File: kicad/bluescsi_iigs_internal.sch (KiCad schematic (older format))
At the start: 26 parts, among them J1 Conn_02x13_Odd_Even, J2 Conn_02x13_Odd_Even, J3 105162-0001, J4 Conn_01x02_Male, Q1 Q_PMOS_GSD, SW1 SW_SPDT, U1 YAAJ_BluePill, U2 UC560x, UCC56xx, U3 UC560x, UCC56xx, U4 AMS1117-5.0

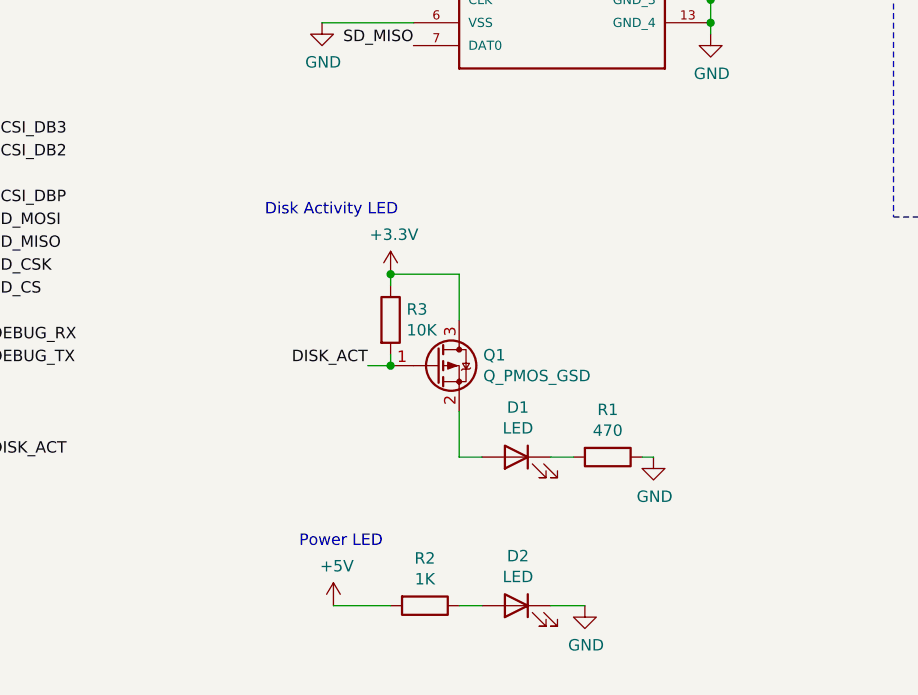
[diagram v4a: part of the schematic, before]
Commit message: Added connector for external activity LED
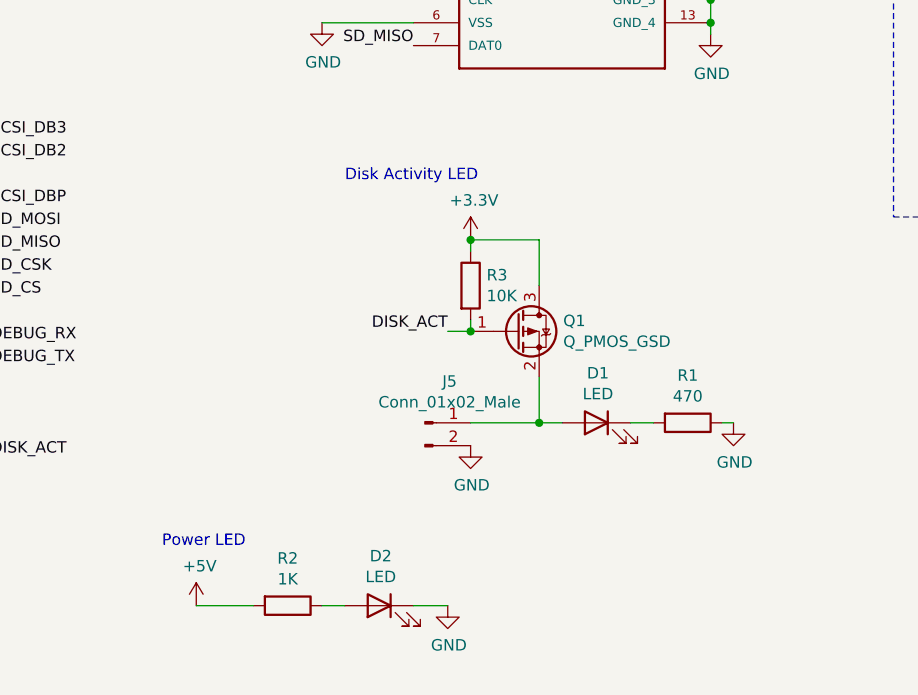
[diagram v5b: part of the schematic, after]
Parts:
- added J5: Conn_01x02_Male, Connector_PinHeader_2.54mm:PinHeader_1x02_P2.54mm_Vertical, symbol Connector:Conn_01x02_Male
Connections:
- net GND: now also J5.2 (Pin_2)
- net at D1.2 (A), Q1.2 (S): now also J5.1 (Pin_1)
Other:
- moved on the sheet: D1, D2, Q1, R1, R2, R3
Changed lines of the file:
@@
 L Device:LED D2
 U 1 1 60631033
-P 5300 7350
-F 0 "D2" H 5293 7567 50  0000 C CNN
-F 1 "LED" H 5293 7476 50  0000 C CNN
-F 2 "LED_SMD:LED_0805_2012Metric_Pad1.15x1.40mm_HandSolder" H 5300 7350 50  0001 C CNN
-F 3 "~" H 5300 7350 50  0001 C CNN
-	1    5300 7350
+P 4700 7350
+F 0 "D2" H 4693 7567 50  0000 C CNN
+F 1 "LED" H 4693 7476 50  0000 C CNN
+F 2 "LED_SMD:LED_0805_2012Metric_Pad1.15x1.40mm_HandSolder" H 4700 7350 50  0001 C CNN
+F 3 "~" H 4700 7350 50  0001 C CNN
+	1    4700 7350
 	-1   0    0    -1
 $EndComp
@@
 L Device:R R2
 U 1 1 60634BDC
-P 4900 7350
-F 0 "R2" V 4693 7350 50  0000 C CNN
-F 1 "1K" V 4784 7350 50  0000 C CNN
-F 2 "Resistor_SMD:R_0805_2012Metric_Pad1.20x1.40mm_HandSolder" V 4830 7350 50  0001 C CNN
-F 3 "~" H 4900 7350 50  0001 C CNN
-	1    4900 7350
+P 4300 7350
+F 0 "R2" V 4093 7350 50  0000 C CNN
+F 1 "1K" V 4184 7350 50  0000 C CNN
+F 2 "Resistor_SMD:R_0805_2012Metric_Pad1.20x1.40mm_HandSolder" V 4230 7350 50  0001 C CNN
+F 3 "~" H 4300 7350 50  0001 C CNN
+	1    4300 7350
 	0    1    1    0
 $EndComp
@@
 L power:GND #PWR0111
 U 1 1 60635DA0
-P 5600 7350
-F 0 "#PWR0111" H 5600 7100 50  0001 C CNN
-F 1 "GND" H 5605 7177 50  0000 C CNN
-F 2 "" H 5600 7350 50  0001 C CNN
-F 3 "" H 5600 7350 50  0001 C CNN
-	1    5600 7350
-	1    0    0    -1
-$EndComp
-Wire Wire Line
-	5450 7350 5600 7350
+P 5000 7350
+F 0 "#PWR0111" H 5000 7100 50  0001 C CNN
+F 1 "GND" H 5005 7177 50  0000 C CNN
+F 2 "" H 5000 7350 50  0001 C CNN
+F 3 "" H 5000 7350 50  0001 C CNN
+	1    5000 7350
+	1    0    0    -1
+$EndComp
+Wire Wire Line
+	4850 7350 5000 7350
 $Comp
 L power:+5V #PWR0113
 U 1 1 60637375
-P 4500 7350
-F 0 "#PWR0113" H 4500 7200 50  0001 C CNN
-F 1 "+5V" H 4515 7523 50  0000 C CNN
-F 2 "" H 4500 7350 50  0001 C CNN
-F 3 "" H 4500 7350 50  0001 C CNN
-	1    4500 7350
-	1    0    0    -1
-$EndComp
-Wire Wire Line
-	4750 7350 4500 7350
+P 3900 7350
+F 0 "#PWR0113" H 3900 7200 50  0001 C CNN
+F 1 "+5V" H 3915 7523 50  0000 C CNN
+F 2 "" H 3900 7350 50  0001 C CNN
+F 3 "" H 3900 7350 50  0001 C CNN
+	1    3900 7350
+	1    0    0    -1
+$EndComp
+Wire Wire Line
+	4150 7350 3900 7350
 $Comp
 L power:GND #PWR0114
@@
 DISK_ACT
 Wire Wire Line
-	5050 7350 5150 7350
-Text Label 4650 6300 2    50   ~ 0
+	4450 7350 4550 7350
+Text Label 5000 6150 2    50   ~ 0
 DISK_ACT
 $Comp
 L Device:R R1
 U 1 1 606332E3
-P 5700 6700
-F 0 "R1" V 5493 6700 50  0000 C CNN
-F 1 "470" V 5584 6700 50  0000 C CNN
-F 2 "Resistor_SMD:R_0805_2012Metric_Pad1.20x1.40mm_HandSolder" V 5630 6700 50  0001 C CNN
-F 3 "~" H 5700 6700 50  0001 C CNN
-	1    5700 6700
+P 6050 6550
+F 0 "R1" V 5843 6550 50  0000 C CNN
+F 1 "470" V 5934 6550 50  0000 C CNN
+F 2 "Resistor_SMD:R_0805_2012Metric_Pad1.20x1.40mm_HandSolder" V 5980 6550 50  0001 C CNN
+F 3 "~" H 6050 6550 50  0001 C CNN
+	1    6050 6550
 	0    1    1    0
 $EndComp
@@
 L Device:LED D1
 U 1 1 60632077
-P 5300 6700
-F 0 "D1" H 5293 6917 50  0000 C CNN
-F 1 "LED" H 5293 6826 50  0000 C CNN
-F 2 "LED_SMD:LED_0805_2012Metric_Pad1.15x1.40mm_HandSolder" H 5300 6700 50  0001 C CNN
-F 3 "~" H 5300 6700 50  0001 C CNN
-	1    5300 6700
+P 5650 6550
+F 0 "D1" H 5643 6767 50  0000 C CNN
+F 1 "LED" H 5643 6676 50  0000 C CNN
+F 2 "LED_SMD:LED_0805_2012Metric_Pad1.15x1.40mm_HandSolder" H 5650 6550 50  0001 C CNN
+F 3 "~" H 5650 6550 50  0001 C CNN
+	1    5650 6550
 	-1   0    0    -1
 $EndComp
-Text Notes 4200 5650 0    50   ~ 0
+Text Notes 4550 5500 0    50   ~ 0
 Disk Activity LED
 Wire Notes Line
@@
 Text Notes 4400 3900 0    50   ~ 0
 MicroSD card slot\nMolex 105162-0001
-Text Notes 4350 7100 0    50   ~ 0
+Text Notes 3750 7100 0    50   ~ 0
 Power LED
 Wire Notes Line
@@
 L Device:Q_PMOS_GSD Q1
 U 1 1 609D8A80
-P 4950 6300
-F 0 "Q1" H 5155 6346 50  0000 L CNN
-F 1 "Q_PMOS_GSD" H 5155 6255 50  0000 L CNN
-F 2 "Package_TO_SOT_SMD:SOT-23" H 5150 6400 50  0001 C CNN
-F 3 "~" H 4950 6300 50  0001 C CNN
-	1    4950 6300
+P 5300 6150
+F 0 "Q1" H 5505 6196 50  0000 L CNN
+F 1 "Q_PMOS_GSD" H 5505 6105 50  0000 L CNN
+F 2 "Package_TO_SOT_SMD:SOT-23" H 5500 6250 50  0001 C CNN
+F 3 "~" H 5300 6150 50  0001 C CNN
+	1    5300 6150
 	1    0    0    -1
 $EndComp
@@
 L power:+3.3V #PWR0126
 U 1 1 609DCA9E
-P 4750 5900
-F 0 "#PWR0126" H 4750 5750 50  0001 C CNN
-F 1 "+3.3V" H 4765 6073 50  0000 C CNN
-F 2 "" H 4750 5900 50  0001 C CNN
-F 3 "" H 4750 5900 50  0001 C CNN
-	1    4750 5900
+P 5100 5750
+F 0 "#PWR0126" H 5100 5600 50  0001 C CNN
+F 1 "+3.3V" H 5115 5923 50  0000 C CNN
+F 2 "" H 5100 5750 50  0001 C CNN
+F 3 "" H 5100 5750 50  0001 C CNN
+	1    5100 5750
 	1    0    0    -1
 $EndComp
@@
 L Device:R R3
 U 1 1 609DE44B
-P 4750 6100
-F 0 "R3" H 4820 6146 50  0000 L CNN
-F 1 "10K" H 4820 6055 50  0000 L CNN
-F 2 "Resistor_SMD:R_0805_2012Metric_Pad1.20x1.40mm_HandSolder" V 4680 6100 50  0001 C CNN
-F 3 "~" H 4750 6100 50  0001 C CNN
-	1    4750 6100
-	1    0    0    -1
-$EndComp
-Wire Wire Line
-	4750 5900 5050 5900
-Wire Wire Line
-	4650 6300 4750 6300
-Wire Wire Line
-	5050 6700 5150 6700
-Wire Wire Line
-	5050 6500 5050 6700
-Wire Wire Line
-	5450 6700 5550 6700
+P 5100 5950
+F 0 "R3" H 5170 5996 50  0000 L CNN
+F 1 "10K" H 5170 5905 50  0000 L CNN
+F 2 "Resistor_SMD:R_0805_2012Metric_Pad1.20x1.40mm_HandSolder" V 5030 5950 50  0001 C CNN
+F 3 "~" H 5100 5950 50  0001 C CNN
+	1    5100 5950
+	1    0    0    -1
+$EndComp
+Wire Wire Line
+	5100 5750 5400 5750
+Wire Wire Line
+	5000 6150 5100 6150
+Wire Wire Line
+	5400 6550 5500 6550
+Wire Wire Line
+	5400 6350 5400 6550
+Wire Wire Line
+	5800 6550 5900 6550
 $Comp
 L power:GND #PWR0127
 U 1 1 609F55CD
-P 5900 6700
-F 0 "#PWR0127" H 5900 6450 50  0001 C CNN
-F 1 "GND" H 5905 6527 50  0000 C CNN
-F 2 "" H 5900 6700 50  0001 C CNN
-F 3 "" H 5900 6700 50  0001 C CNN
-	1    5900 6700
-	1    0    0    -1
-$EndComp
-Wire Wire Line
-	5850 6700 5900 6700
-Wire Wire Line
-	5050 5900 5050 6100
-Wire Wire Line
-	4750 5900 4750 5950
-Connection ~ 4750 5900
-Wire Wire Line
-	4750 6250 4750 6300
-Connection ~ 4750 6300
+P 6250 6550
+F 0 "#PWR0127" H 6250 6300 50  0001 C CNN
+F 1 "GND" H 6255 6377 50  0000 C CNN
+F 2 "" H 6250 6550 50  0001 C CNN
+F 3 "" H 6250 6550 50  0001 C CNN
+	1    6250 6550
+	1    0    0    -1
+$EndComp
+Wire Wire Line
+	6200 6550 6250 6550
+Wire Wire Line
+	5400 5750 5400 5950
+Wire Wire Line
+	5100 5750 5100 5800
+Connection ~ 5100 5750
+Wire Wire Line
+	5100 6100 5100 6150
+Connection ~ 5100 6150
+$Comp
+L Connector:Conn_01x02_Male J5
+U 1 1 60AA760E
+P 4900 6550
+F 0 "J5" H 5008 6731 50  0000 C CNN
+F 1 "Conn_01x02_Male" H 5008 6640 50  0000 C CNN
+F 2 "Connector_PinHeader_2.54mm:PinHeader_1x02_P2.54mm_Vertical" H 4900 6550 50  0001 C CNN
+F 3 "~" H 4900 6550 50  0001 C CNN
+	1    4900 6550
+	1    0    0    -1
+$EndComp
+Wire Wire Line
+	5100 6550 5400 6550
+Connection ~ 5400 6550
+$Comp
+L power:GND #PWR0128
+U 1 1 60AA99DB
+P 5100 6650
+F 0 "#PWR0128" H 5100 6400 50  0001 C CNN
+F 1 "GND" H 5105 6477 50  0000 C CNN
+F 2 "" H 5100 6650 50  0001 C CNN
+F 3 "" H 5100 6650 50  0001 C CNN
+	1    5100 6650
+	1    0    0    -1
+$EndComp
 $EndSCHEMATC

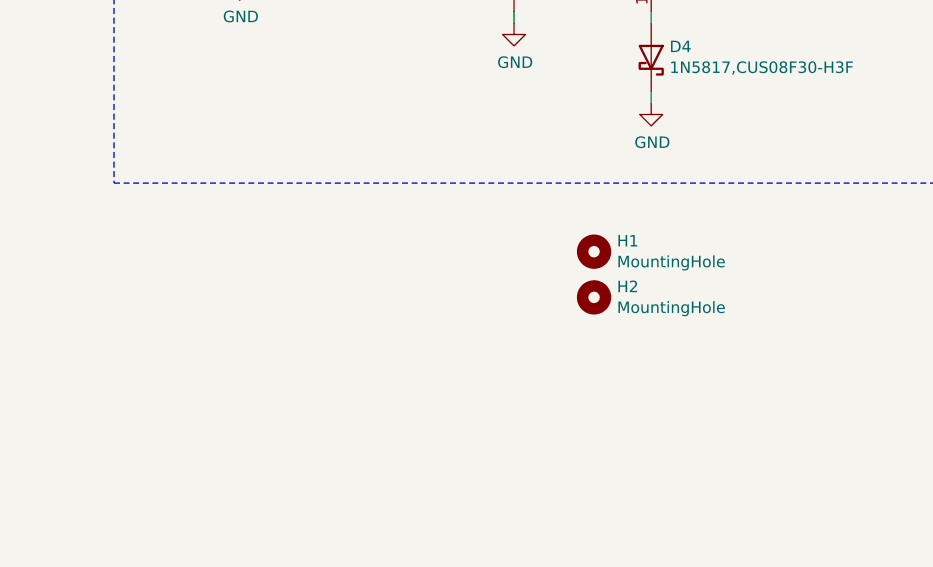
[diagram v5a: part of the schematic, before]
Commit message: Replace mounting holes with Keystone 7774 brackets
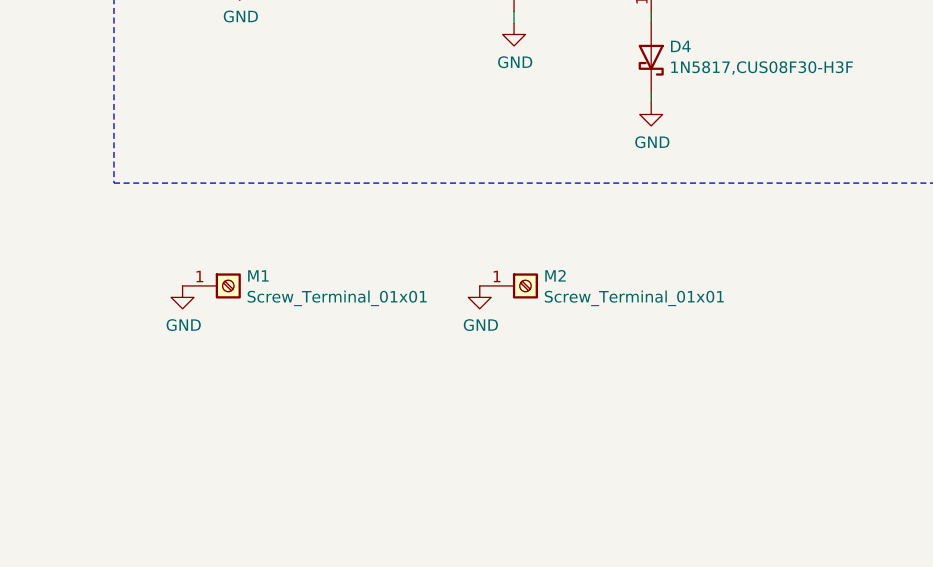
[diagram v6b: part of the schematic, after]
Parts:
- removed H1, H2: MountingHole, MountingHole:MountingHole_3mm, symbol Mechanical:MountingHole
- added M1, M2: Screw_Terminal_01x01, my library:keystone-7774, symbol Connector:Screw_Terminal_01x01
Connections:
- net GND: now also M1.1 (Pin_1), M2.1 (Pin_1)
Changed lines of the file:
@@
 NoConn ~ 4850 4300
-$Comp
-L Mechanical:MountingHole H1
-U 1 1 60629B83
-P 9050 5950
-F 0 "H1" H 9150 5996 50  0000 L CNN
-F 1 "MountingHole" H 9150 5905 50  0000 L CNN
-F 2 "MountingHole:MountingHole_3mm" H 9050 5950 50  0001 C CNN
-F 3 "~" H 9050 5950 50  0001 C CNN
-	1    9050 5950
-	1    0    0    -1
-$EndComp
-$Comp
-L Mechanical:MountingHole H2
-U 1 1 6062A4C4
-P 9050 6150
-F 0 "H2" H 9150 6196 50  0000 L CNN
-F 1 "MountingHole" H 9150 6105 50  0000 L CNN
-F 2 "MountingHole:MountingHole_3mm" H 9050 6150 50  0001 C CNN
-F 3 "~" H 9050 6150 50  0001 C CNN
-	1    9050 6150
-	1    0    0    -1
-$EndComp
 $Comp
 L Device:LED D2
@@
 	1    0    0    -1
 $EndComp
+$Comp
+L power:GND #PWR0130
+U 1 1 609FCFD6
+P 8550 6100
+F 0 "#PWR0130" H 8550 5850 50  0001 C CNN
+F 1 "GND" H 8555 5927 50  0000 C CNN
+F 2 "" H 8550 6100 50  0001 C CNN
+F 3 "" H 8550 6100 50  0001 C CNN
+	1    8550 6100
+	1    0    0    -1
+$EndComp
+$Comp
+L power:GND #PWR0129
+U 1 1 609FBA87
+P 7250 6100
+F 0 "#PWR0129" H 7250 5850 50  0001 C CNN
+F 1 "GND" H 7255 5927 50  0000 C CNN
+F 2 "" H 7250 6100 50  0001 C CNN
+F 3 "" H 7250 6100 50  0001 C CNN
+	1    7250 6100
+	1    0    0    -1
+$EndComp
+$Comp
+L Connector:Screw_Terminal_01x01 M2
+U 1 1 609E648B
+P 8750 6100
+F 0 "M2" H 8830 6142 50  0000 L CNN
+F 1 "Screw_Terminal_01x01" H 8830 6051 50  0000 L CNN
+F 2 "my library:keystone-7774" H 8750 6100 50  0001 C CNN
+F 3 "~" H 8750 6100 50  0001 C CNN
+	1    8750 6100
+	1    0    0    -1
+$EndComp
+$Comp
+L Connector:Screw_Terminal_01x01 M1
+U 1 1 609E5C80
+P 7450 6100
+F 0 "M1" H 7530 6142 50  0000 L CNN
+F 1 "Screw_Terminal_01x01" H 7530 6051 50  0000 L CNN
+F 2 "my library:keystone-7774" H 7450 6100 50  0001 C CNN
+F 3 "~" H 7450 6100 50  0001 C CNN
+	1    7450 6100
+	1    0    0    -1
+$EndComp

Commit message: pth regulator hanging off the side
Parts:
- D3: value 1N5817,1N5817,CUS08F30-H3F -> 1N4001; symbol Device:D_Schottky -> Diode:1N4001
- D4: value 1N5817,CUS08F30-H3F -> 1N4001; symbol Device:D_Schottky -> Diode:1N4001
- U4: value AMS1117-5.0 -> MC7805CT-BP; footprint Package_TO_SOT_SMD:SOT-223-3_TabPin2 -> Package_TO_SOT_THT:TO-220-3_Vertical; symbol Regulator_Linear:AMS1117-5.0 -> Regulator_Linear:L7805
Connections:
- net +12V_AUX: now also U4.1 (IN); no longer U4.3 (VI)
- net REG_OUT: now also U4.3 (OUT); no longer U4.2 (VO)
- net at D4.2 (A): now also U4.2 (GND); no longer U4.1 (GND)
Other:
- note added: "Auxilliary 12V power from IIgs fan connector in case TERMPWR is not available\n\nReverse-protected via D3.\nD4 boosts the output of regulator U4 to compensate for voltage drop of D3.\nHeat-sink recommended."
- note removed: "Auxilliary 12V power from IIgs fan connector in case TERMPWR is not available\n\nReverse-protected via D3.\nD4 boosts the output of regulator U4 to compensate for voltage drop of D3."
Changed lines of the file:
@@
-$EndComp
-$Comp
-L Regulator_Linear:AMS1117-5.0 U4
-U 1 1 608623C0
-P 9300 4600
-F 0 "U4" H 9300 4842 50  0000 C CNN
-F 1 "AMS1117-5.0" H 9300 4751 50  0000 C CNN
-F 2 "Package_TO_SOT_SMD:SOT-223-3_TabPin2" H 9300 4800 50  0001 C CNN
-F 3 "http://www.advanced-monolithic.com/pdf/ds1117.pdf" H 9400 4350 50  0001 C CNN
-	1    9300 4600
-	1    0    0    -1
 $EndComp
 $Comp
@@
 Wire Wire Line
 	9300 4900 9300 4950
-$Comp
-L Device:D_Schottky D3
-U 1 1 6086E55B
-P 10300 4600
-F 0 "D3" H 10300 4383 50  0000 C CNN
-F 1 "1N5817,1N5817,CUS08F30-H3F" H 10300 4474 50  0000 C CNN
-F 2 "Diode_SMD:D_SOD-323_HandSoldering" H 10300 4600 50  0001 C CNN
-F 3 "~" H 10300 4600 50  0001 C CNN
-	1    10300 4600
-	-1   0    0    1
-$EndComp
-$Comp
-L Device:D_Schottky D4
-U 1 1 6086EF1B
-P 9300 5100
-F 0 "D4" V 9346 5180 50  0000 L CNN
-F 1 "1N5817,CUS08F30-H3F" V 9255 5180 50  0000 L CNN
-F 2 "Diode_SMD:D_SOD-323_HandSoldering" H 9300 5100 50  0001 C CNN
-F 3 "~" H 9300 5100 50  0001 C CNN
-	1    9300 5100
-	0    1    -1   0
-$EndComp
 Wire Wire Line
 	9300 5250 9300 5300
@@
 Wire Notes Line
 	9000 700  6350 700
-Text Notes 7400 4200 0    50   ~ 0
-Auxilliary 12V power from IIgs fan connector in case TERMPWR is not available\n\nReverse-protected via D3.\nD4 boosts the output of regulator U4 to compensate for voltage drop of D3.
 Wire Notes Line
 	6950 3750 6950 5650
@@
 	1    0    0    -1
 $EndComp
+$Comp
+L Diode:1N4001 D3
+U 1 1 6086E55B
+P 10300 4600
+F 0 "D3" H 10300 4383 50  0000 C CNN
+F 1 "1N4001" H 10300 4474 50  0000 C CNN
+F 2 "Diode_SMD:D_SOD-323_HandSoldering" H 10300 4600 50  0001 C CNN
+F 3 "~" H 10300 4600 50  0001 C CNN
+	1    10300 4600
+	-1   0    0    1
+$EndComp
+$Comp
+L Diode:1N4001 D4
+U 1 1 6086EF1B
+P 9300 5100
+F 0 "D4" V 9346 5180 50  0000 L CNN
+F 1 "1N4001" V 9255 5180 50  0000 L CNN
+F 2 "Diode_SMD:D_SOD-323_HandSoldering" H 9300 5100 50  0001 C CNN
+F 3 "~" H 9300 5100 50  0001 C CNN
+	1    9300 5100
+	0    1    -1   0
+$EndComp
+Text Notes 7400 4200 0    50   ~ 0
+Auxilliary 12V power from IIgs fan connector in case TERMPWR is not available\n\nReverse-protected via D3.\nD4 boosts the output of regulator U4 to compensate for voltage drop of D3.\nHeat-sink recommended.
+$Comp
+L Regulator_Linear:L7805 U4
+U 1 1 608623C0
+P 9300 4600
+F 0 "U4" H 9300 4842 50  0000 C CNN
+F 1 "MC7805CT-BP" H 9300 4751 50  0000 C CNN
+F 2 "Package_TO_SOT_THT:TO-220-3_Vertical" H 9300 4800 50  0001 C CNN
+F 3 "https://www.mouser.com/datasheet/2/258/MC7805CT(TO-220)-E-1626349.pdf" H 9400 4350 50  0001 C CNN
+	1    9300 4600
+	1    0    0    -1
+$EndComp
